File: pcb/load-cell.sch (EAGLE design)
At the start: 1 part, among them IC1 HX711

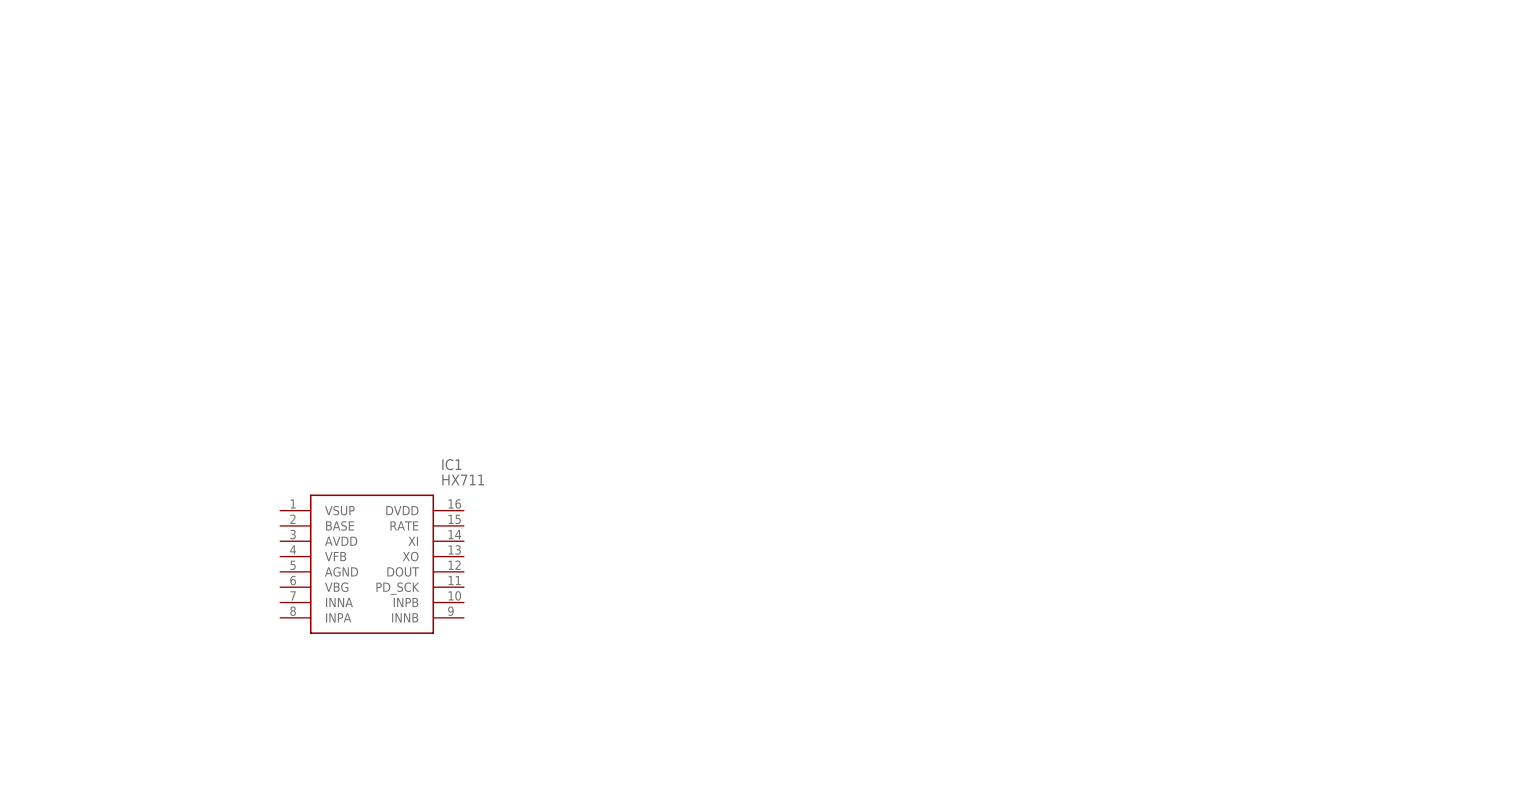
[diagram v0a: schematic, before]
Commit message: Updated the PCB Schematic: 80% complete. Added PCB reference.
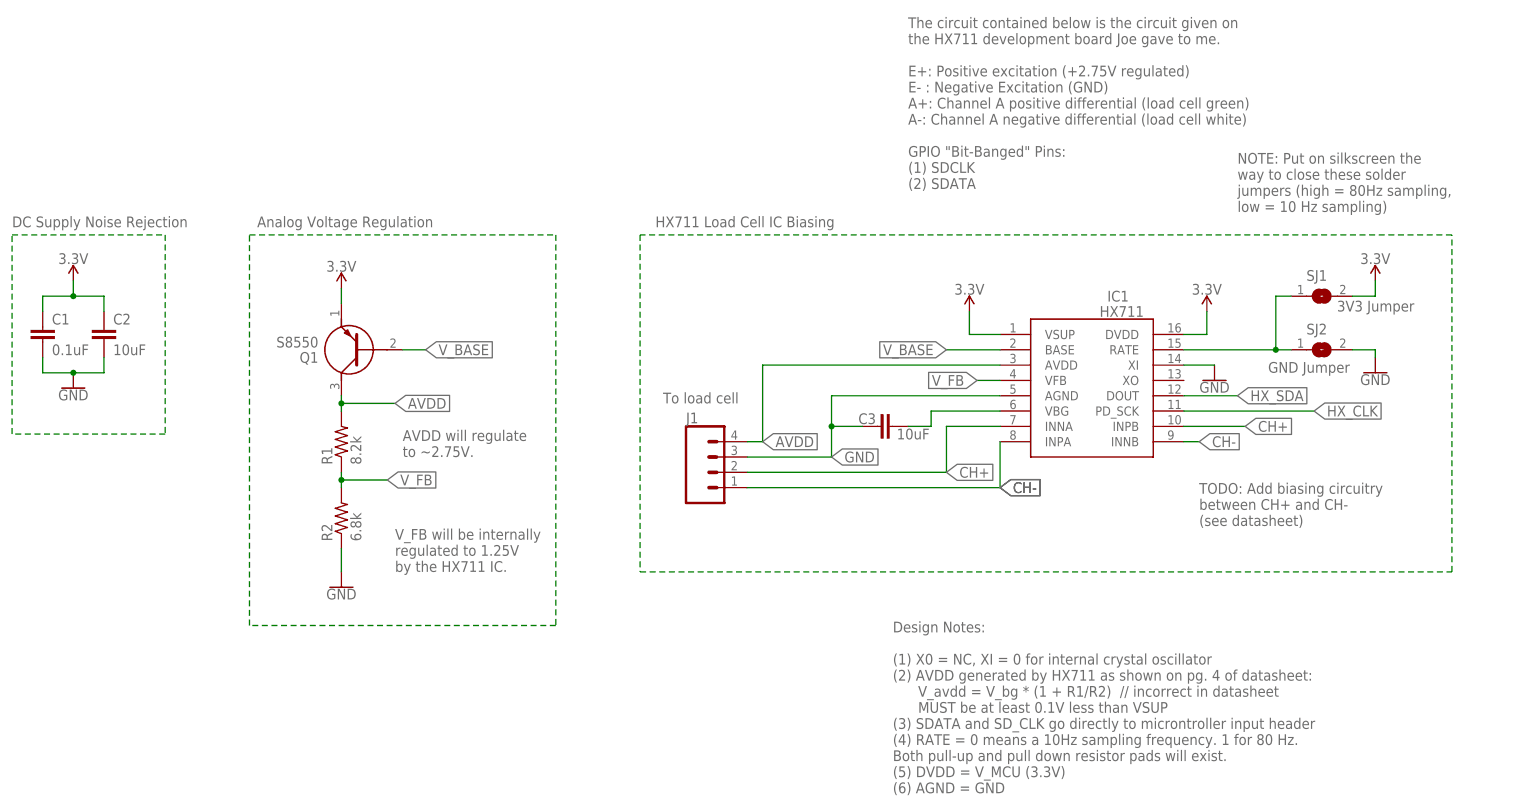
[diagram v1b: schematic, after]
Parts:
- added C1: 0.1uF, LinnesLab-Passives:CAPACITOR0603
- added C2, C3: 10uF, LinnesLab-Passives:CAPACITOR0603
- added J1: (no value), LinnesLab-Connectors:CONN_04
- added Q1: S8550, SamacSys_Parts:S8550
- added R1: 8.2k, LinnesLab-Passives:RESISTOR0603
- added R2: 6.8k, LinnesLab-Passives:RESISTOR0603
- added SJ1: 3V3 Jumper, jumper:SJ
- added SJ2: GND Jumper, jumper:SJ
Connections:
- new net 3.3V: C1.1, C2.1, IC1.DVDD, IC1.VSUP, Q1.E, SJ1.2
- new net AVDD: IC1.AVDD, J1.4, Q1.C, R1.2
- new net CH+: IC1.INNA, IC1.INPB, J1.2
- new net CH-: IC1.INNB, IC1.INPA, J1.1
- new net GND: C1.2, C2.2, C3.1, IC1.AGND, IC1.XI, J1.3, R2.1, SJ2.2
- new net HX_CLK: IC1.PD_SCK
- new net HX_SDA: IC1.DOUT
- new net N$2: C3.2, IC1.VBG
- new net N$7: IC1.RATE, SJ1.1, SJ2.1
- new net V_BASE: IC1.BASE, Q1.B
- new net V_FB: IC1.VFB, R1.1, R2.2
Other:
- note added: "AVDD will regulate to ~2.75V."
- note added: "Analog Voltage Regulation"
- note added: "DC Supply Noise Rejection"
- note added: "Design Notes: (1) X0 = NC, XI = 0 for internal crystal oscillator (2) AVDD generated by HX711 as shown on pg. 4 of datasheet: V_avdd = V_bg * (1 + R1/R2) // incorrect in datasheet MUST be at least 0.1V less than VSUP (3) SDATA and SD_CLK go directly to microntroller input header (4) RATE = 0 means a 10Hz sampling frequency. 1 for 80 Hz. Both pull-up and pull down resistor pads will exist. (5) DVD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"
- note added: "HX711 Load Cell IC Biasing"
- note added: "NOTE: Put on silkscreen the way to close these solder jumpers (high = 80Hz sampling, low = 10 Hz sampling)"
- note added: "TODO: Add biasing circuitry between CH+ and CH- (see datasheet)"
- note added: "The circuit contained below is the circuit given on the HX711 development board Joe gave to me. E+: Positive excitation (+2.75V regulated) E- : Negative Excitation (GND) A+: Channel A positive differential (load cell green) A-: Channel A negative differential (load cell white) GPIO "Bit-Banged" Pins: (1) SDCLK (2) SDATA"
- note added: "To load cell"
- note added: "V_FB will be internally regulated to 1.25V by the HX711 IC."
- moved on the sheet: IC1
